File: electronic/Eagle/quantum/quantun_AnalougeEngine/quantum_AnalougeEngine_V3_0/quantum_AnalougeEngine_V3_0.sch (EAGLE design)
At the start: 167 parts, among them IC1 OP275, IC10 NE5532D, IC2 NE5532D, IC3 NE5532D, IC4 OP275, IC5 NE5532D, IC6 NE5532D, IC7 NE5532D, IC8 OP275, IC9 TL072, K5 RELAY_EE2-5NU, K6 RELAY_EE2-5NU, K7 RELAY_EE2-5NU, K8 RELAY_EE2-5NU, U1 NUCLEO-F429ZI, U12 ULN2003, U4 THAT1240, U6 THAT1240, U7 THAT1240, U8 THAT1240

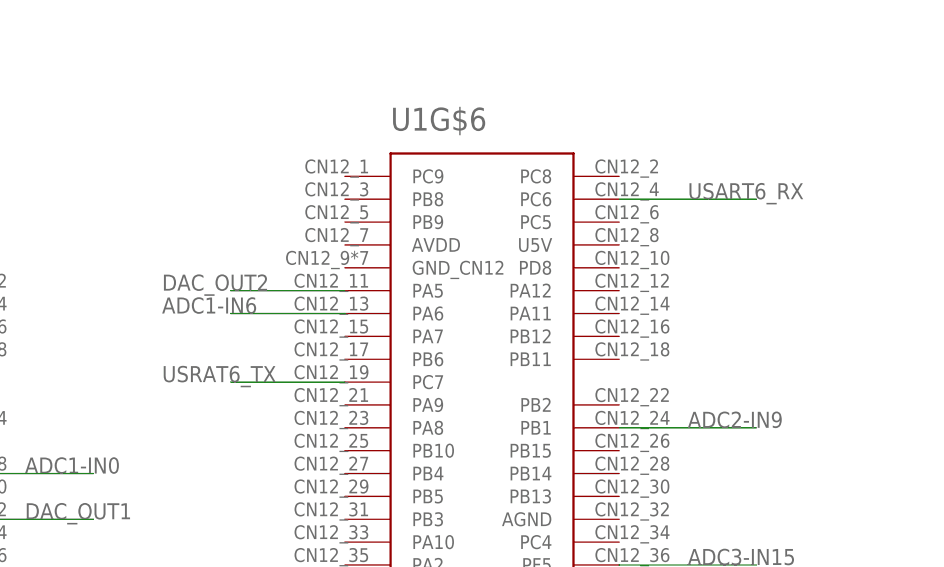
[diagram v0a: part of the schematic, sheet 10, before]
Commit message: - UART6 Transmit implemented - DMA ADC now fully working - implemented OSCmessageINTSend();
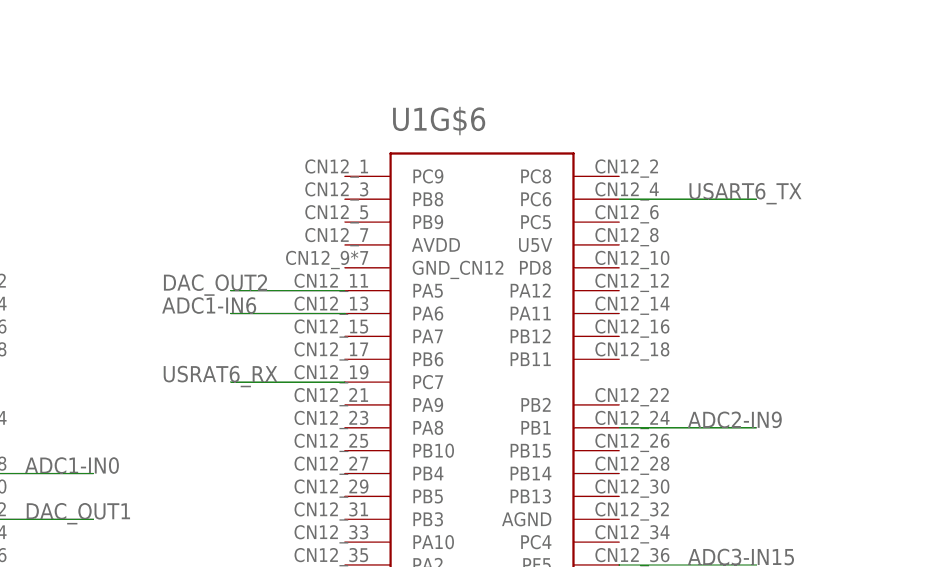
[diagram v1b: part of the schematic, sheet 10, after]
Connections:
- net USART6_RX renamed USART6_TX
- net USRAT6_TX renamed USRAT6_RX
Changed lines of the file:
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@@
 </segment>
 </net>
-<net name="USART6_RX" class="0">
+<net name="USART6_TX" class="0">
 <segment>
 <pinref part="U1" gate="G$6" pin="PC6"/>
@@
 </segment>
 </net>
-<net name="USRAT6_TX" class="0">
+<net name="USRAT6_RX" class="0">
 <segment>
 <pinref part="U1" gate="G$6" pin="PC7"/>
